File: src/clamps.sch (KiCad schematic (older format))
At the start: 36 parts, among them P1 CONN_01X12, U1 LM741, U2 LM741, U3 LM741, U4 LM741, U5 LM741, U6 LM741

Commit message: update
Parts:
- added R?: R, symbol R
- added U?: DAC8734, symbol DAC8734
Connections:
- net +VE: now also U?.26 (AV-DD), U?.35 (AV-DD)
- net -VE: now also U?.28 (AV-SS), U?.33 (AV-SS)
- net GND: now also U?.27 (AGND)
- net REF: now also U?.30 (REF-A), U?.31 (REF-B)
- new net: R?.2, U?.47 (AIN)
- new net 3.3V: U?.10 (UNI/BIP-A), U?.13 (IOV-DD), U?.14 (DV-DD), U?.48 (UNI/BIP-B)
- new net DGND: U?.11 (DGND)
- new net REFGND: R?.1, U?.18 (SGND-0), U?.20 (SGND-1), U?.29 (REFGND-A), U?.32 (REFGND-B), U?.41 (SGND-3), U?.43 (SGND-2)
- no-connect marks 16 -> 24
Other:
- moved on the sheet: C1, C10, C11, C12, C2, C3, C4, C5, C6, C7, C8, C9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

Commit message: update
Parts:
- added R? (x2): R, symbol R
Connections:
- wire segments 99 -> 178
- no-connect marks 24 -> 25
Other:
- moved on the sheet: D1, D2, D3, D4, R1, R10, R11, R12, R13, R2, R3, R4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

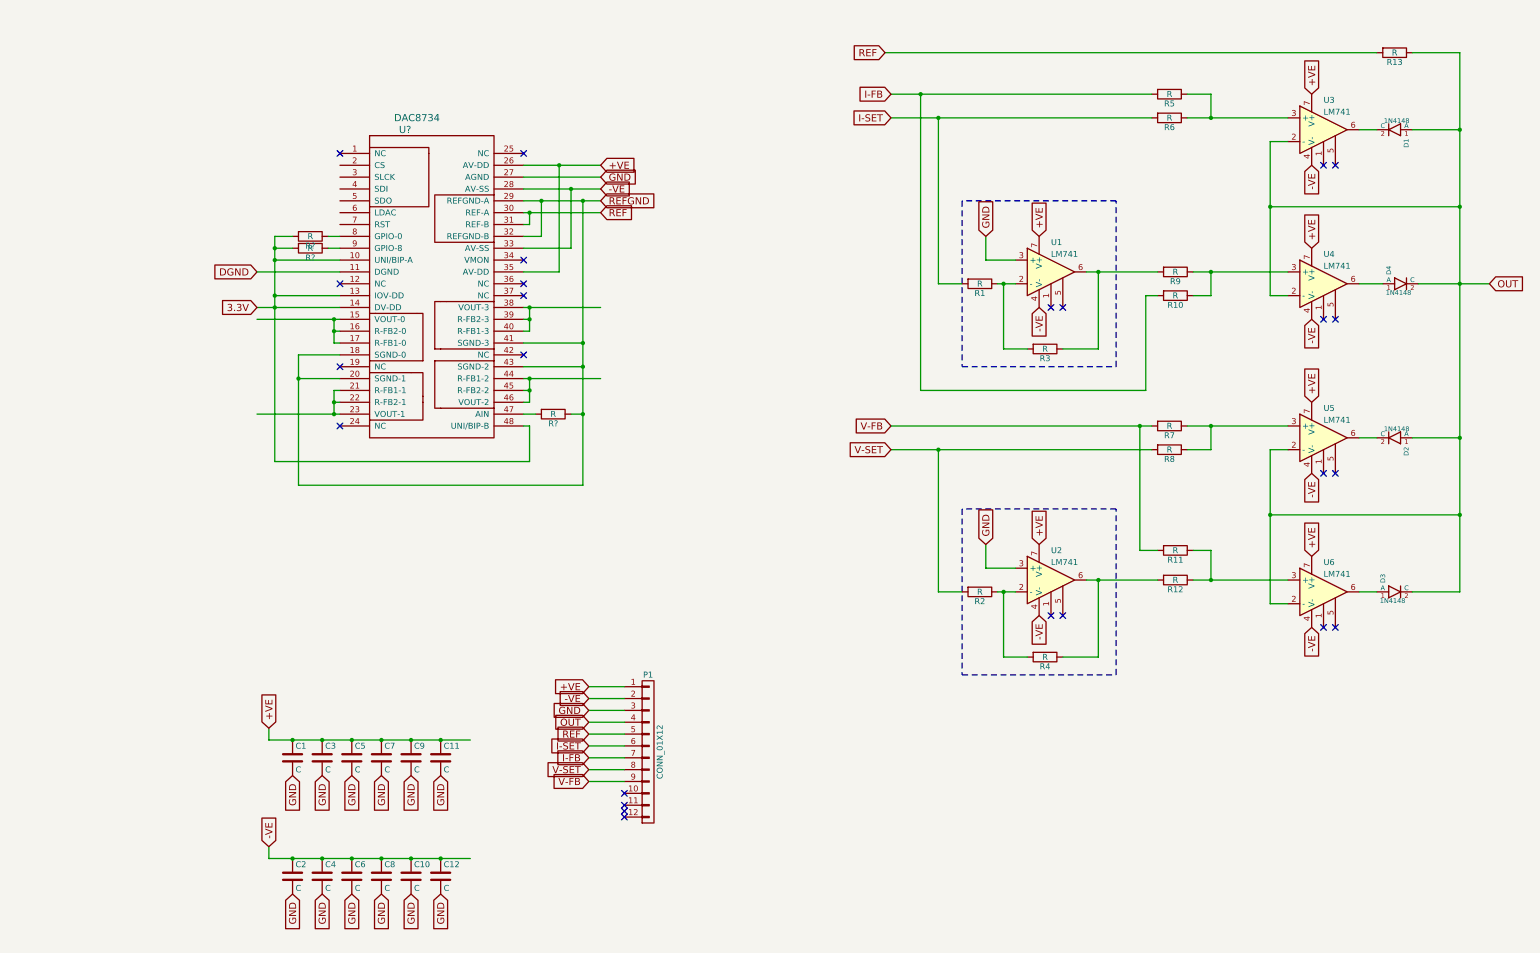
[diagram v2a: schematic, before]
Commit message: fix and annotate clamps
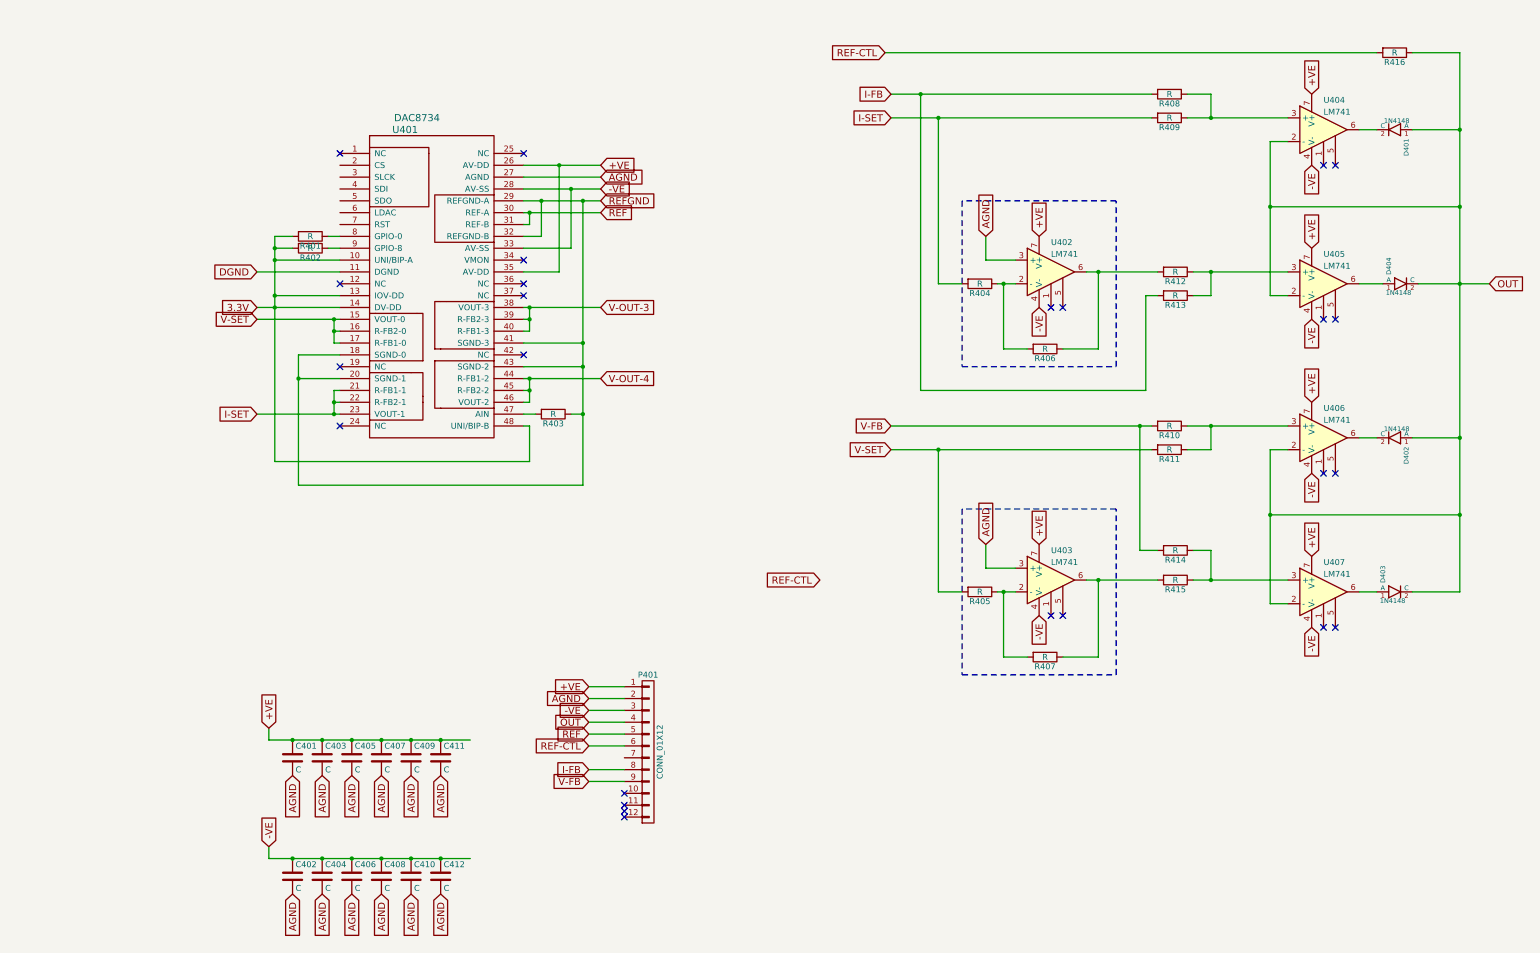
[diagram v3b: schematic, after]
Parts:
- gave numbers to parts that had none: 4
- renumbered C1 to C401, C2 to C402, C3 to C403, C4 to C404, C5 to C405, C6 to C406, C7 to C407, C8 to C408, C9 to C409, C10 to C410, C11 to C411, C12 to C412, D1 to D401, D2 to D402, D3 to D403, D4 to D404, P1 to P401, R1 to R404, R2 to R405, R3 to R406, R4 to R407, R5 to R408, R6 to R409, R7 to R410, R8 to R411, R9 to R412, R10 to R413, R11 to R414, R12 to R415, R13 to R416, U1 to U402, U2 to U403, U3 to U404, U4 to U405, U5 to U406, U6 to U407
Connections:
- net labels added: AGND, REF-CTL, V-OUT-3, V-OUT-4
- net labels removed: GND
- wire segments 178 -> 123

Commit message: initial clamps pcb
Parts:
- R401, R402, R403: footprint (none) -> Resistors_SMD:R_1206
- U401: footprint (none) -> Housings_QFP:TQFP-48_7x7mm_Pitch0.5mm
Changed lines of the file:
@@
 F 0 "R403" V 5130 4200 50  0000 C CNN
 F 1 "R" V 5050 4200 50  0000 C CNN
-F 2 "" V 4980 4200 50  0000 C CNN
+F 2 "Resistors_SMD:R_1206" V 4980 4200 50  0001 C CNN
 F 3 "" H 5050 4200 50  0000 C CNN
 	1    5050 4200
@@
 F 0 "R401" V 3080 2700 50  0000 C CNN
 F 1 "R" V 3000 2700 50  0000 C CNN
-F 2 "" V 2930 2700 50  0000 C CNN
+F 2 "Resistors_SMD:R_1206" V 2930 2700 50  0001 C CNN
 F 3 "" H 3000 2700 50  0000 C CNN
 	1    3000 2700
@@
 F 0 "R402" V 3080 2800 50  0000 C CNN
 F 1 "R" V 3000 2800 50  0000 C CNN
-F 2 "" V 2930 2800 50  0000 C CNN
+F 2 "Resistors_SMD:R_1206" V 2930 2800 50  0001 C CNN
 F 3 "" H 3000 2800 50  0000 C CNN
 	1    3000 2800
@@
 F 0 "U401" H 3800 2800 60  0000 C CNN
 F 1 "DAC8734" H 3900 2900 60  0000 C CNN
-F 2 "" H 3850 2300 60  0001 C CNN
+F 2 "Housings_QFP:TQFP-48_7x7mm_Pitch0.5mm" H 3850 2300 60  0001 C CNN
 F 3 "" H 3850 2300 60  0001 C CNN
 	1    3850 2300
@@
 Text GLabel 5450 3900 2    60   Input ~ 0
 V-OUT-4
-Text GLabel 7300 5600 0    60   Input ~ 0
-REF-CTL
 Text GLabel 5350 7000 0    60   Input ~ 0
 REF-CTL
